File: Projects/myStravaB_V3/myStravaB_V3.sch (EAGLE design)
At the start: 82 parts, among them IC1 TPS63051RMWT, IC2 BMD-340-A-R, Q2 BSS138BKW, T2 BC847, U1 FXOS8700CQR1, U2 MCP73831, Y3 32.768kHz

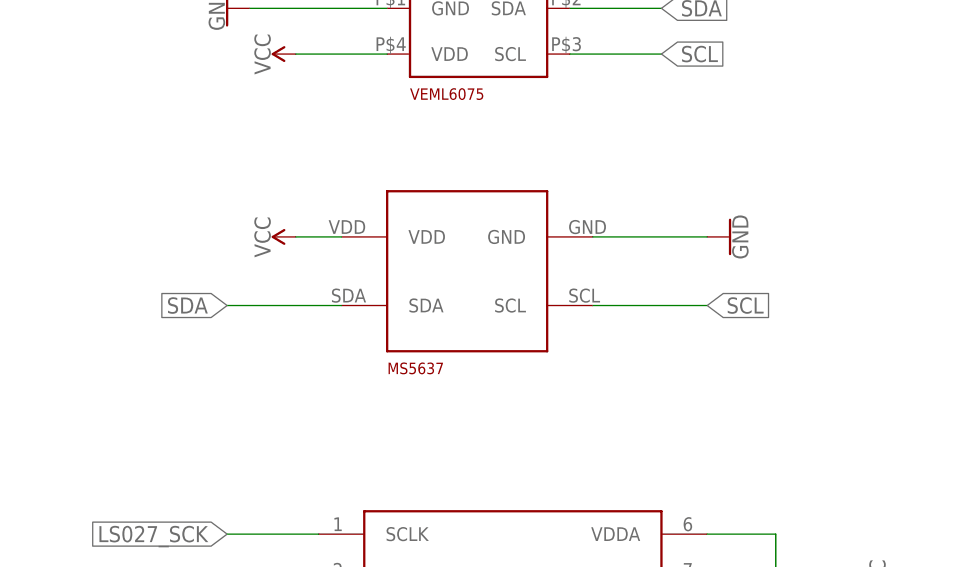
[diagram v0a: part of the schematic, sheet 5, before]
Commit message: Replaced barometer in strava V3
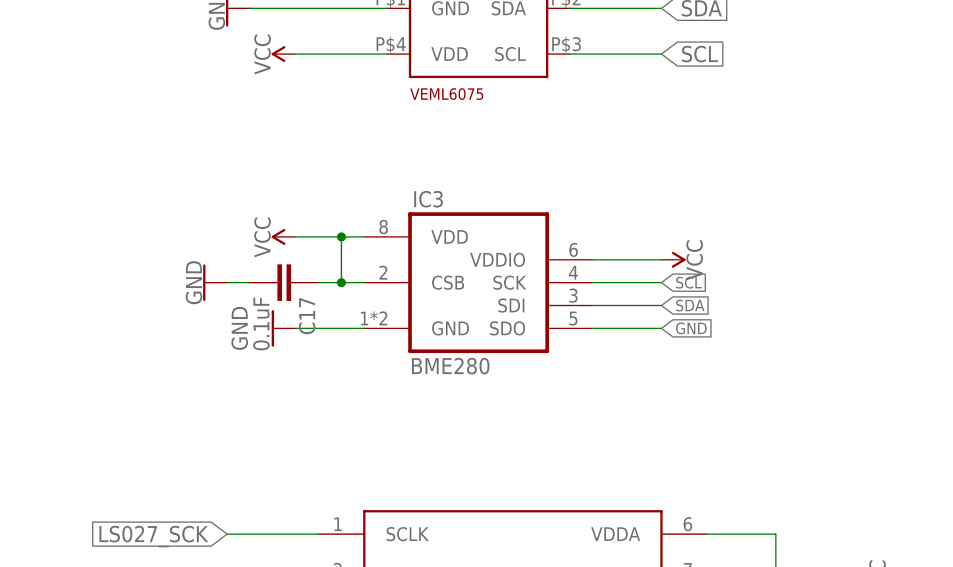
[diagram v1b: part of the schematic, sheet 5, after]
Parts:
- removed MS1: MS5637, MS5637:MS5637
- added C17: 0.1uF, SparkFun-Capacitors:0.1UF-0603-25V-(+80/-20%)
- added IC3: BME280, bosch-bme280:BME280
- added R5: 100k, rcl:R-US_R0603
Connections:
- new net N$3: R5.2, U$1G$2.G
- net GND: now also C17.2, IC3.GND, IC3.SDO; no longer MS1.GND
- net INV: now also R5.1; no longer U$1G$2.G
- net SCL: now also IC3.SCK; no longer MS1.SCL
- net SDA: now also IC3.SDI; no longer MS1.SDA
- net VCC: now also C17.1, IC3.CSB, IC3.VDD, IC3.VDDIO; no longer MS1.VDD

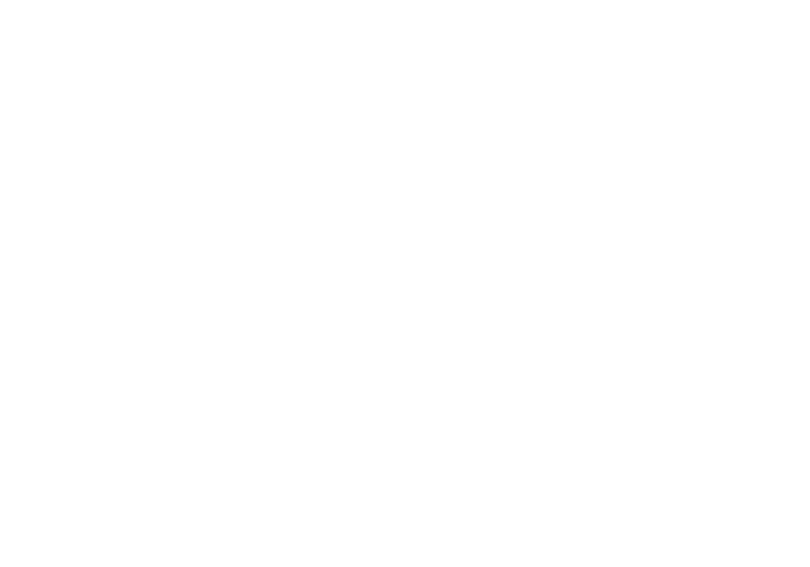
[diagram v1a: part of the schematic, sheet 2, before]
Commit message: Corrected BMD340 footprint Update the board with FRAM, bme280 and new pins assignments
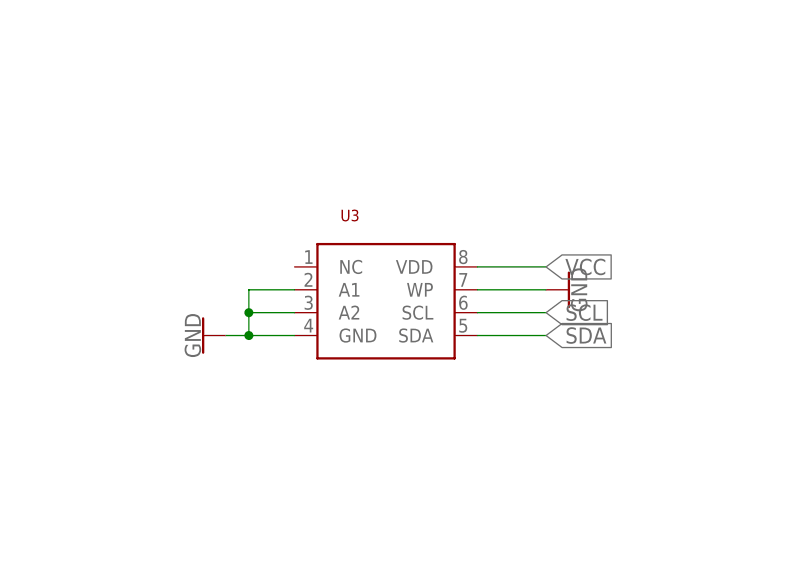
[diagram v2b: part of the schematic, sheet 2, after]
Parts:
- added U3: (no value), FRAM:TWI_FRAM
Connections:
- net FIX: now also IC2.P1.14; no longer IC2.P0.07
- net GND: now also U3.A1, U3.A2, U3.GND, U3.WP
- net GPS_RST: now also IC2.P0.03; no longer IC2.P0.05
- net GPS_RX: now also IC2.P0.05; no longer IC2.P0.03
- net GPS_TX: now also IC2.P0.07; no longer IC2.P1.14
- net SCL: now also U3.SCL
- net SDA: now also U3.SDA
- net SPI_MI: now also IC2.P0.24; no longer IC2.P0.23
- net SPI_SCK: now also IC2.P0.18; no longer IC2.P0.2
- net SST_CS: now also IC2.P0.22; no longer IC2.P0.18
- net SST_WP: now also IC2.P0.23; no longer IC2.P0.22
- net VCC: now also U3.VDD
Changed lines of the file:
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@@
 <?xml version="1.0" encoding="utf-8"?>
 <!DOCTYPE eagle SYSTEM "eagle.dtd">
-<eagle version="9.2.2">
+<eagle version="9.3.0">
 <drawing>
 <settings>
-<setting alwaysvectorfont="yes"/>
+<setting alwaysvectorfont="no"/>
 <setting keepoldvectorfont="yes"/>
 <setting verticaltext="up"/>
@@
 <part name="GND47" library="SparkFun-PowerSymbols" deviceset="GND" device=""/>
 <part name="R5" library="rcl" library_urn="urn:adsk.eagle:library:334" deviceset="R-US_" device="R0603" package3d_urn="urn:adsk.eagle:package:23555/2" value="100k"/>
+<part name="U3" library="FRAM" deviceset="TWI_FRAM" device=""/>
+<part name="GND48" library="SparkFun-PowerSymbols" deviceset="GND" device=""/>
+<part name="GND49" library="SparkFun-PowerSymbols" deviceset="GND" device=""/>
 </parts>
 <sheets>
@@
 <net name="GPS_RX" class="0">
 <segment>
-<pinref part="IC2" gate="G$1" pin="P0.03"/>
-<wire x1="12.7" y1="302.26" x2="5.08" y2="302.26" width="0.1524" layer="91"/>
-<label x="5.08" y="302.26" size="1.27" layer="95" rot="R180" xref="yes"/>
+<pinref part="IC2" gate="G$1" pin="P0.05"/>
+<wire x1="12.7" y1="297.18" x2="5.08" y2="297.18" width="0.1524" layer="91"/>
+<label x="5.08" y="297.18" size="1.27" layer="95" rot="R180" xref="yes"/>
 </segment>
 </net>
@@
 <pinref part="IC2" gate="G$1" pin="P0.26"/>
 <label x="5.08" y="332.74" size="1.27" layer="95" rot="R180" xref="yes"/>
-</segment>
-</net>
-<net name="FIX" class="0">
-<segment>
-<pinref part="IC2" gate="G$1" pin="P0.07"/>
-<wire x1="12.7" y1="292.1" x2="5.08" y2="292.1" width="0.1524" layer="91"/>
-<label x="5.08" y="292.1" size="1.27" layer="95" rot="R180" xref="yes"/>
 </segment>
 </net>
@@
 <net name="GPS_TX" class="0">
 <segment>
-<pinref part="IC2" gate="G$1" pin="P1.14"/>
-<wire x1="45.72" y1="276.86" x2="50.8" y2="276.86" width="0.1524" layer="91"/>
-<label x="50.8" y="276.86" size="1.27" layer="95" xref="yes"/>
+<pinref part="IC2" gate="G$1" pin="P0.07"/>
+<wire x1="12.7" y1="292.1" x2="5.08" y2="292.1" width="0.1524" layer="91"/>
+<label x="5.08" y="292.1" size="1.27" layer="95" rot="R180" xref="yes"/>
 </segment>
 </net>
@@
 </segment>
 </net>
-<net name="GPS_RST" class="0">
-<segment>
-<pinref part="IC2" gate="G$1" pin="P0.05"/>
-<wire x1="12.7" y1="297.18" x2="5.08" y2="297.18" width="0.1524" layer="91"/>
-<label x="5.08" y="297.18" size="1.27" layer="95" rot="R180" xref="yes"/>
-</segment>
-</net>
 <net name="SST_CS" class="0">
+<segment>
+<pinref part="IC2" gate="G$1" pin="P0.22"/>
+<wire x1="45.72" y1="335.28" x2="53.34" y2="335.28" width="0.1524" layer="91"/>
+<label x="53.34" y="335.28" size="1.27" layer="95" xref="yes"/>
+</segment>
+</net>
+<net name="SPI_SCK" class="0">
 <segment>
 <pinref part="IC2" gate="G$1" pin="P0.18"/>
@@
 </segment>
 </net>
-<net name="SPI_SCK" class="0">
-<segment>
-<pinref part="IC2" gate="G$1" pin="P0.2"/>
-<wire x1="45.72" y1="340.36" x2="53.34" y2="340.36" width="0.1524" layer="91"/>
-<label x="53.34" y="340.36" size="1.27" layer="95" xref="yes"/>
-</segment>
-</net>
 <net name="SPI_MI" class="0">
+<segment>
+<pinref part="IC2" gate="G$1" pin="P0.24"/>
+<wire x1="45.72" y1="330.2" x2="53.34" y2="330.2" width="0.1524" layer="91"/>
+<label x="53.34" y="330.2" size="1.27" layer="95" xref="yes"/>
+</segment>
+</net>
+<net name="SST_WP" class="0">
 <segment>
 <pinref part="IC2" gate="G$1" pin="P0.23"/>
@@
 </segment>
 </net>
-<net name="SST_WP" class="0">
-<segment>
-<pinref part="IC2" gate="G$1" pin="P0.22"/>
-<wire x1="45.72" y1="335.28" x2="53.34" y2="335.28" width="0.1524" layer="91"/>
-<label x="53.34" y="335.28" size="1.27" layer="95" xref="yes"/>
-</segment>
-</net>
 <net name="SST_HOLD" class="0">
 <segment>
@@
 <wire x1="45.72" y1="345.44" x2="53.34" y2="345.44" width="0.1524" layer="91"/>
 <label x="53.34" y="345.44" size="1.27" layer="95" xref="yes"/>
+</segment>
+</net>
+<net name="GPS_RST" class="0">
+<segment>
+<pinref part="IC2" gate="G$1" pin="P0.03"/>
+<wire x1="12.7" y1="302.26" x2="5.08" y2="302.26" width="0.1524" layer="91"/>
+<label x="5.08" y="302.26" size="1.27" layer="95" rot="R180" xref="yes"/>
+</segment>
+</net>
+<net name="FIX" class="0">
+<segment>
+<pinref part="IC2" gate="G$1" pin="P1.14"/>
+<wire x1="45.72" y1="276.86" x2="50.8" y2="276.86" width="0.1524" layer="91"/>
+<label x="50.8" y="276.86" size="1.27" layer="95" xref="yes"/>
 </segment>
 </net>
@@
 <attribute name="VALUE" x="45.72" y="38.354" size="1.778" layer="96" rot="R180" align="top-center"/>
 </instance>
+<instance part="U3" gate="G$1" x="15.24" y="83.82" smashed="yes">
+<attribute name="NAME" x="10.16" y="93.98" size="1.27" layer="94"/>
+<attribute name="VALUE" x="10.16" y="76.2" size="1.27" layer="94"/>
+</instance>
+<instance part="GND48" gate="1" x="-5.08" y="81.28" smashed="yes" rot="R270">
+<attribute name="VALUE" x="-5.334" y="81.28" size="1.778" layer="96" rot="R270" align="top-center"/>
+</instance>
+<instance part="GND49" gate="1" x="35.56" y="86.36" smashed="yes" rot="R90">
+<attribute name="VALUE" x="35.814" y="86.36" size="1.778" layer="96" rot="R90" align="top-center"/>
+</instance>
 </instances>
 <busses>
@@
 <label x="-154.94" y="30.48" size="1.778" layer="95" rot="R180" xref="yes"/>
 </segment>
+<segment>
+<pinref part="U3" gate="G$1" pin="SDA"/>
+<wire x1="25.4" y1="81.28" x2="33.02" y2="81.28" width="0.1524" layer="91"/>
+<label x="33.02" y="81.28" size="1.778" layer="95" xref="yes"/>
+</segment>
 </net>
 <net name="SCL" class="0">
@@
 <wire x1="-129.54" y1="35.56" x2="-154.94" y2="35.56" width="0.1524" layer="91"/>
 <label x="-154.94" y="35.56" size="1.778" layer="95" rot="R180" xref="yes"/>
+</segment>
+<segment>
+<pinref part="U3" gate="G$1" pin="SCL"/>
+<wire x1="25.4" y1="83.82" x2="33.02" y2="83.82" width="0.1524" layer="91"/>
+<label x="33.02" y="83.82" size="1.778" layer="95" xref="yes"/>
 </segment>
 </net>
@@
 <pinref part="C18" gate="G$1" pin="2"/>
 <wire x1="45.72" y1="35.56" x2="45.72" y2="33.02" width="0.1524" layer="91"/>
+</segment>
+<segment>
+<pinref part="U3" gate="G$1" pin="GND"/>
+<wire x1="5.08" y1="81.28" x2="0" y2="81.28" width="0.1524" layer="91"/>
+<pinref part="GND48" gate="1" pin="GND"/>
+<pinref part="U3" gate="G$1" pin="A1"/>
+<wire x1="0" y1="81.28" x2="-2.54" y2="81.28" width="0.1524" layer="91"/>
+<wire x1="5.08" y1="86.36" x2="0" y2="86.36" width="0.1524" layer="91"/>
+<pinref part="U3" gate="G$1" pin="A2"/>
+<wire x1="5.08" y1="83.82" x2="0" y2="83.82" width="0.1524" layer="91"/>
+<wire x1="0" y1="86.36" x2="0" y2="83.82" width="0.1524" layer="91"/>
+<wire x1="0" y1="83.82" x2="0" y2="81.28" width="0.1524" layer="91"/>
+<junction x="0" y="83.82"/>
+<junction x="0" y="81.28"/>
+</segment>
+<segment>
+<pinref part="U3" gate="G$1" pin="WP"/>
+<wire x1="25.4" y1="86.36" x2="33.02" y2="86.36" width="0.1524" layer="91"/>
+<pinref part="GND49" gate="1" pin="GND"/>
 </segment>
 </net>
@@
 <junction x="45.72" y="22.86"/>
 </segment>
-</net>
+<segment>
+<pinref part="U3" gate="G$1" pin="VDD"/>
+<wire x1="25.4" y1="88.9" x2="33.02" y2="88.9" width="0.1524" layer="91"/>
+<label x="33.02" y="88.9" size="1.778" layer="95" xref="yes"/>
+</segment>
+</net>

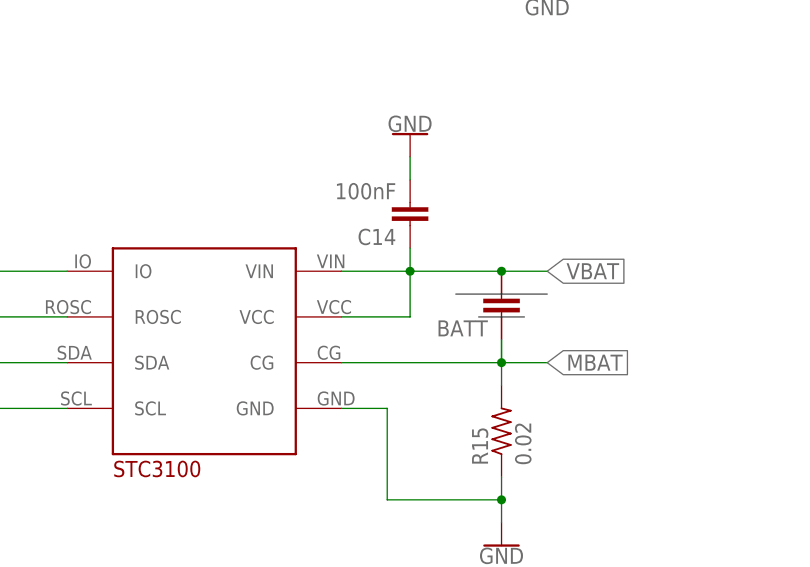
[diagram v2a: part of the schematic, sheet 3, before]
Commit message: Thermal routing for BMD340
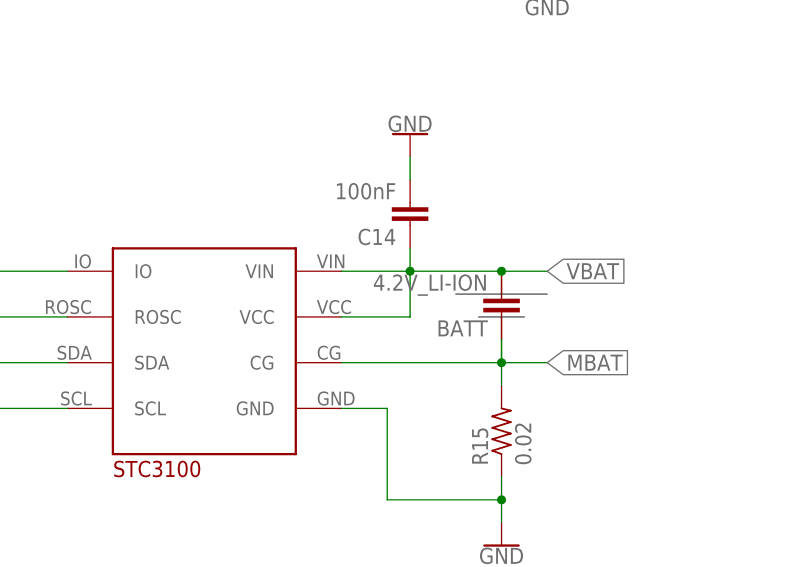
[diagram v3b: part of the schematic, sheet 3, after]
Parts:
- BATT: value (none) -> 4.2V_LI-ION
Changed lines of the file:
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@@
 <part name="R21" library="rcl" library_urn="urn:adsk.eagle:library:334" deviceset="R-US_" device="R0603" package3d_urn="urn:adsk.eagle:package:23555/2" value="200k 0.1%"/>
 <part name="GND29" library="SparkFun-PowerSymbols" deviceset="GND" device=""/>
-<part name="BATT" library="rcl" library_urn="urn:adsk.eagle:library:334" deviceset="C-EU" device="C1210" package3d_urn="urn:adsk.eagle:package:23619/2"/>
+<part name="BATT" library="rcl" library_urn="urn:adsk.eagle:library:334" deviceset="C-EU" device="C1210" package3d_urn="urn:adsk.eagle:package:23619/2" value="4.2V_LI-ION"/>
 <part name="T2" library="nxp_60" deviceset="BC847" device=""/>
 <part name="R25" library="rcl" library_urn="urn:adsk.eagle:library:334" deviceset="R-US_" device="R0603" package3d_urn="urn:adsk.eagle:package:23555/2" value="100k"/>
@@
 <segment>
 <pinref part="R31" gate="G$1" pin="2"/>
+<label x="20.32" y="393.7" size="1.27" layer="95" rot="R270" xref="yes"/>
 <wire x1="25.4" y1="393.7" x2="20.32" y2="393.7" width="0.1524" layer="91"/>
-<label x="20.32" y="393.7" size="1.27" layer="95" rot="R270" xref="yes"/>
 </segment>
 <segment>
@@
 <segment>
 <pinref part="R30" gate="G$1" pin="2"/>
+<label x="12.7" y="393.7" size="1.27" layer="95" rot="R270" xref="yes"/>
 <wire x1="7.62" y1="393.7" x2="12.7" y2="393.7" width="0.1524" layer="91"/>
-<label x="12.7" y="393.7" size="1.27" layer="95" rot="R270" xref="yes"/>
-</segment>
-<segment>
-<wire x1="12.7" y1="332.74" x2="5.08" y2="332.74" width="0.1524" layer="91"/>
+</segment>
+<segment>
 <pinref part="IC2" gate="G$1" pin="P0.26"/>
 <label x="5.08" y="332.74" size="1.27" layer="95" rot="R180" xref="yes"/>
+<wire x1="12.7" y1="332.74" x2="5.08" y2="332.74" width="0.1524" layer="91"/>
 </segment>
 </net>
@@
 <segment>
 <pinref part="IC2" gate="G$1" pin="P0.17"/>
+<label x="53.34" y="347.98" size="1.27" layer="95" xref="yes"/>
 <wire x1="45.72" y1="347.98" x2="53.34" y2="347.98" width="0.1524" layer="91"/>
-<label x="53.34" y="347.98" size="1.27" layer="95" xref="yes"/>
 </segment>
 </net>
@@
 <segment>
 <pinref part="IC2" gate="G$1" pin="P0.19"/>
+<label x="53.34" y="342.9" size="1.27" layer="95" xref="yes"/>
 <wire x1="45.72" y1="342.9" x2="53.34" y2="342.9" width="0.1524" layer="91"/>
-<label x="53.34" y="342.9" size="1.27" layer="95" xref="yes"/>
 </segment>
 </net>
@@
 <segment>
 <pinref part="IC2" gate="G$1" pin="P0.16"/>
+<label x="5.08" y="264.16" size="1.27" layer="95" rot="R180" xref="yes"/>
 <wire x1="12.7" y1="264.16" x2="5.08" y2="264.16" width="0.1524" layer="91"/>
-<label x="5.08" y="264.16" size="1.27" layer="95" rot="R180" xref="yes"/>
 </segment>
 </net>
@@
 <segment>
 <pinref part="IC2" gate="G$1" pin="P0.22"/>
+<label x="53.34" y="335.28" size="1.27" layer="95" xref="yes"/>
 <wire x1="45.72" y1="335.28" x2="53.34" y2="335.28" width="0.1524" layer="91"/>
-<label x="53.34" y="335.28" size="1.27" layer="95" xref="yes"/>
 </segment>
 </net>
@@
 <segment>
 <pinref part="IC2" gate="G$1" pin="P0.24"/>
+<label x="53.34" y="330.2" size="1.27" layer="95" xref="yes"/>
 <wire x1="45.72" y1="330.2" x2="53.34" y2="330.2" width="0.1524" layer="91"/>
-<label x="53.34" y="330.2" size="1.27" layer="95" xref="yes"/>
-</segment>
-</net>
+</segment>
+</net>

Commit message: Strava V3 FRAM value set
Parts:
- U3: value (none) -> FM24CL16B
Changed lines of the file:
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@@
 <part name="GND47" library="SparkFun-PowerSymbols" deviceset="GND" device=""/>
 <part name="R5" library="rcl" library_urn="urn:adsk.eagle:library:334" deviceset="R-US_" device="R0603" package3d_urn="urn:adsk.eagle:package:23555/2" value="100k"/>
-<part name="U3" library="FRAM" deviceset="TWI_FRAM" device=""/>
+<part name="U3" library="FRAM" deviceset="TWI_FRAM" device="" value="FM24CL16B"/>
 <part name="GND48" library="SparkFun-PowerSymbols" deviceset="GND" device=""/>
 <part name="GND49" library="SparkFun-PowerSymbols" deviceset="GND" device=""/>

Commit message: Simplified strava
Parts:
- removed BTNC1, BTND1, BTNG1: SKRMAAE010, SPST:SKRMAAE010
- removed C3, C5: 100nF, SparkFun-Capacitors:4.7UF0603
- removed C38, C39: (no value), rcl:C-EUC0603
- removed C4: 10uF, SparkFun-Capacitors:4.7UF0603
- removed D1: BAT54C, diode:BAT54C
- removed L2: TBD, SparkFun-Resistors:4.7KOHM-0603-1/10W-1%
- removed R10, R25, R5, R8: 100k, rcl:R-US_R0603
- removed R11: 300k, rcl:R-US_R0603
- removed R20: 47, SparkFun-Resistors:4.7KOHM-0603-1/10W-1%
- removed R22: 80, SparkFun-Resistors:4.7KOHM-0603-1/10W-1%
- removed R26: 10k, rcl:R-US_R0603
- removed R9: 47k, rcl:R-US_R0603
- removed T2: BC847, nxp_60:BC847
- removed U$1: DMG6602, nxp_60:DMG6602
- removed U$14: VEML6075, VEML6075:VEML6075
- removed U$17, U$18, U$19: KPA-2106SECK, KPA_LED:KPA-2106SECK
- removed U$7: PROG_SMD, Prog:PROG_SMD
- added B1: MICRO-SD_FOOTPRINT, SD_Card:MICRO-SD_FOOTPRINT
- added J1, SD: 47571-0001, SD_Card:47571-0001
- added M1, M2: (no value), MOSFET:GEN_NCH
- added SPST1, SPST2, SPST3: PTS526SK08, SPST:PTS526SK08
- added U4: (no value), PowerSupplies:TPS7A05XX
- C1: value 1uF -> 4.7uF
- R3, R4: value 10k -> 100k
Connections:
- removed net BCK_LED_TR: R20.2, U$19.P$1, U$6.IO
- removed net INT1: IC2.P0.28, U1.INT1
- removed net INT2: U1.INT2
- removed net INT_PSWITCH: D1.A2, R10.2, R11.1, T2.C
- removed net INV: C1.1, C3.1, R5.1, R8.1, U$1G$1.D
- removed net KILL_NRF: IC2.P0.12, R25.2, R26.2
- removed net N$12: R25.1, T2.B
- removed net N$15: C4.1, R11.2, U$1G$1.G
- removed net N$16: R22.2, U$19.P$2
- removed net N$17: R20.1, U$17.P$1, U$18.P$1
- removed net N$3: R5.2, U$1G$2.G
- removed net NRF_BTNC: C5.2, D1.A1, IC2.P0.13, R9.1
- removed net PW_EN: C4.2, IC1.EN, L4.VDD, R10.1, R14.1, R18.2, R4.1, U$1G$2.D
- removed net RF_IN: C38.1, L2.2, U$5.RF_IN
- new net 5V: L4.VDD, R18.2, U$16.VDD, U$16.VDDA, U4.OUT
- new net FXOS_INT1: IC2.P1.02, U1.INT1
- new net POW_EN: IC1.EN, M2.D, R14.1, U4.EN
- new net SD_CLK: IC2.P0.27, SD.CLK
- new net SD_CS: IC2.P0.26, SD.CS
- new net SD_MISO: IC2.P0.28, SD.MISO
- new net SD_MOSI: IC2.P0.25, SD.MOSI
- new net SWON: M2.G, R3.1, U$6.IO
- net ANT: now also U$5.RF_IN; no longer C39.1, L2.1
- net BTNC: now also IC2.P0.13, SPST2.P$2; no longer BTNC1.P$2, C1.2, D1.CC, R3.1
- net BTND: now also SPST3.P$2; no longer BTND1.P$2
- net BTNG: now also SPST1.P$2; no longer BTNG1.P$2
- net FXOS_RST: now also IC2.P1.03; no longer IC2.P0.27
- net GND: now also C1.1, J1.GND, J1.MECH, R4.2, SD.GND, SPST1.P$1, SPST2.P$1, SPST3.P$1, U4.GND; no longer BTNC1.P$1, BTND1.P$1, BTNG1.P$1, C3.2, C38.2, C39.2, C5.1, R26.1, T2.E, U$14.GND, U$1G$1.S, U$7.GND
- net SCL: now also IC2.P1.01; no longer IC2.P0.25, U$14.SCL
- net SDA: now also IC2.P1.00; no longer IC2.P0.26, U$14.SDA
- net SWDCLK: now also J1.D2; no longer U$7.SWDCLK
- net SWDIO: now also J1.D1; no longer U$7.SWDIO
- net VBAT: now also M1.D, M2.S; no longer D3.A2, R8.2, U$1G$2.S
- net VCC: now also C1.2, J1.VCC, SD.VCC; no longer R22.1, R9.2, U$14.VDD, U$16.VDD, U$16.VDDA, U$17.P$2, U$18.P$2, U$7.VCC
- net VIN: now also M1.S, U4.IN
- net VUSB: now also M1.G, R4.1; no longer R4.2
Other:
- moved on the sheet: BATT, C14, C15, C16, C17, C19, C21, C32, C33, C43, D3, IC2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
